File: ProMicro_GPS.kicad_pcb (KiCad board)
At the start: 2 copper layers, 17.8 x 30.5 mm, 30 parts, among them J1 uFL, J2 Coax, U1 MAX-8C, U2 MPU-9250

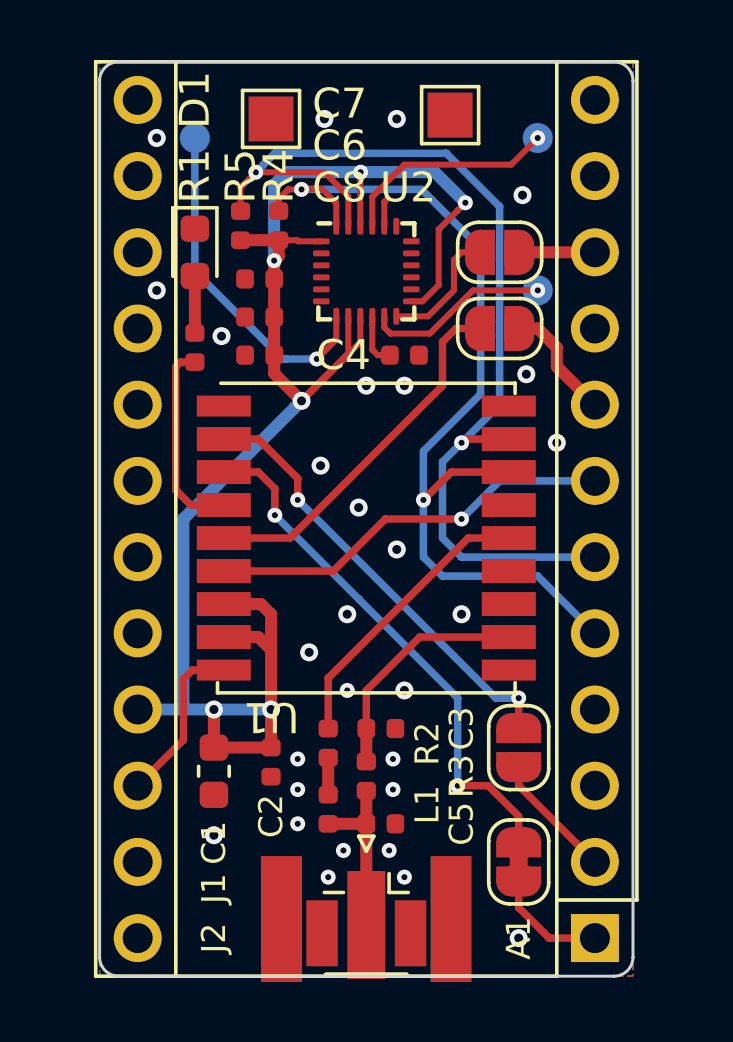
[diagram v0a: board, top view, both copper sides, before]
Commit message: docu in layout
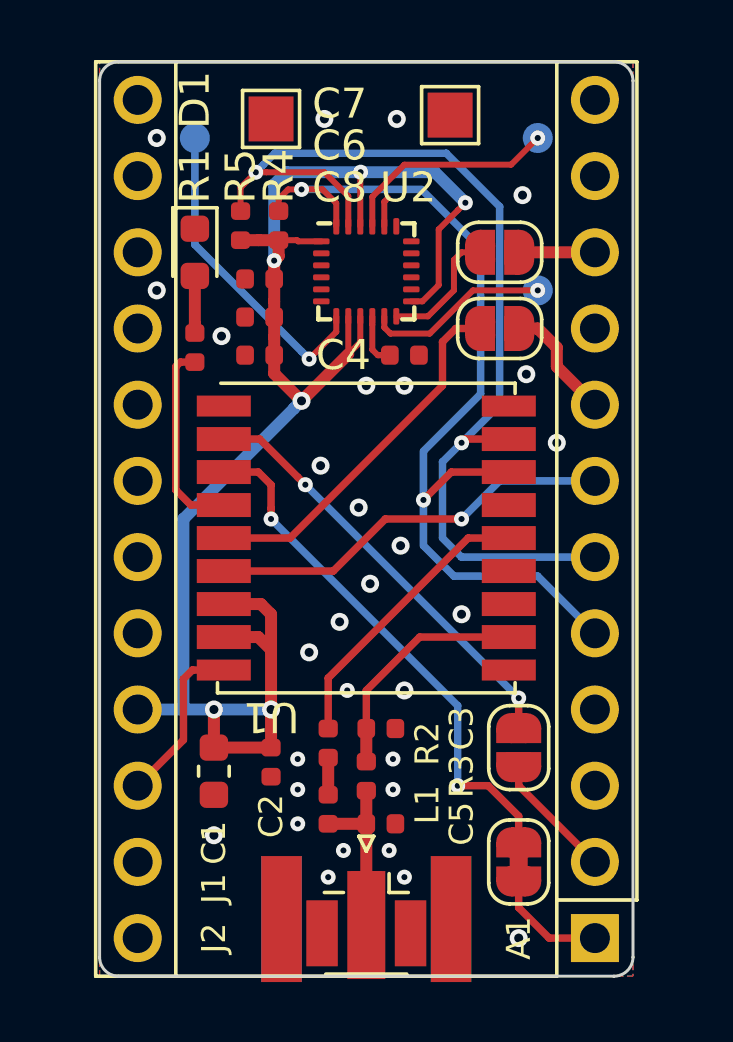
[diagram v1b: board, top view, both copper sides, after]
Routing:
- net Net-(TP3-Pad1): track 11.4 -> 10.7 mm
- net GND: vias 29 -> 30
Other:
- board text added: "3V3"
- board text added: "GND"
- board text added: "GPS_EXTINT"
- board text added: "MPU_INT"
- board text added: "RXD"
- board text added: "SCL"
- board text added: "SDA"
- board text added: "TXD"
- board text added: "VBAT"
- board text added: "v2.3"
- board text added: "~RESET"
- board text removed: "v2.1"

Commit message: variant management
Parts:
- C2: value 100nF -> 100n
- JP1: value SolderJumper_2_Open -> Jumper_NC_Small; footprint Jumper:SolderJumper-2_P1.3mm_Open_RoundedPad1.0x1.5mm -> Jumper:SolderJumper-2_P1.3mm_Bridged_RoundedPad1.0x1.5mm
- JP2: value SolderJumper_2_Open -> Jumper_NO_Small
- JP3: value Jumper_NO_Small -> SolderJumper_2_Open
- JP4: value Jumper_NC_Small -> SolderJumper_2_Open; footprint Jumper:SolderJumper-2_P1.3mm_Bridged_RoundedPad1.0x1.5mm -> Jumper:SolderJumper-2_P1.3mm_Open_RoundedPad1.0x1.5mm
- moved JP4 20.3 mm to (135.3, 88.9), turned to 0 degrees
- moved JP1 17.8 mm to (135.9, 109.2), turned to 90 degrees
- moved JP2 16.5 mm to (135.9, 105.4), turned to 90 degrees
- moved JP3 14.0 mm to (135.3, 91.4), turned to 180 degrees
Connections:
- A1 pad 11: (no net) -> D8
- A1 pad 12: (no net) -> D9
- A1 pad 13: (no net) -> D10
- A1 pad 14: (no net) -> D16
- A1 pad 15: (no net) -> D14
- A1 pad 16: (no net) -> D15
- A1 pad 17: (no net) -> A0
- A1 pad 18: (no net) -> A1
- A1 pad 19: (no net) -> A2
- A1 pad 20: (no net) -> A3
- A1 pad 24: (no net) -> Net-(A1-Pad24)
- A1 pad 3: (no net) -> Net-(A1-Pad3)
- A1 pad 9: (no net) -> D6
- JP1 pad 1: D5 -> D1
- JP2 pad 1: Net-(JP2-Pad1) -> D0
- JP2 pad 2: D7 -> Net-(JP2-Pad2)
- JP3 pad 1: D0 -> D5
- JP4 pad 1: D1 -> Net-(JP4-Pad1)
- JP4 pad 2: Net-(JP4-Pad2) -> D7
- U1 pad 13: (no net) -> Net-(U1-Pad13)
- U1 pad 15: (no net) -> Net-(U1-Pad15)
- U1 pad 18: (no net) -> Net-(U1-Pad18)
- U1 pad 2: Net-(JP3-Pad2) -> Net-(JP2-Pad2)
- U1 pad 3: Net-(JP4-Pad2) -> Net-(JP1-Pad2)
- U1 pad 5: Net-(JP1-Pad2) -> Net-(JP3-Pad2)
- U2 pad 12: Net-(JP2-Pad1) -> Net-(JP4-Pad1)
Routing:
- net Net-(JP4-Pad2): track 17.7 -> 0.00 mm, vias 2 -> 0
- net Net-(JP2-Pad2): track 0.00 -> 14.4 mm, vias 0 -> 2
- net Net-(JP1-Pad2): track 12.3 -> 17.7 mm, vias 0 -> 2
- net Net-(JP4-Pad1): track 0.00 -> 4.27 mm
- net Net-(JP2-Pad1): track 4.27 -> 0.00 mm
- net Net-(JP3-Pad2): track 14.4 -> 12.3 mm, vias 2 -> 0
- net GND: vias 30 -> 32

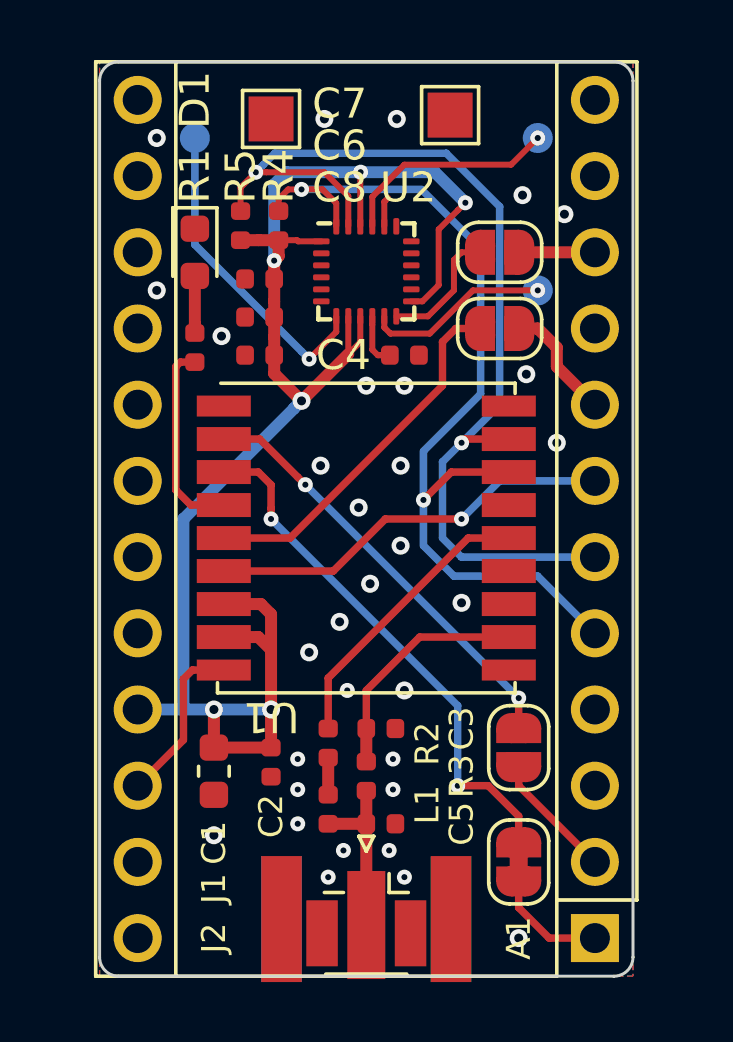
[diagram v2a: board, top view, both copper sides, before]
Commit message: add mouting brackets
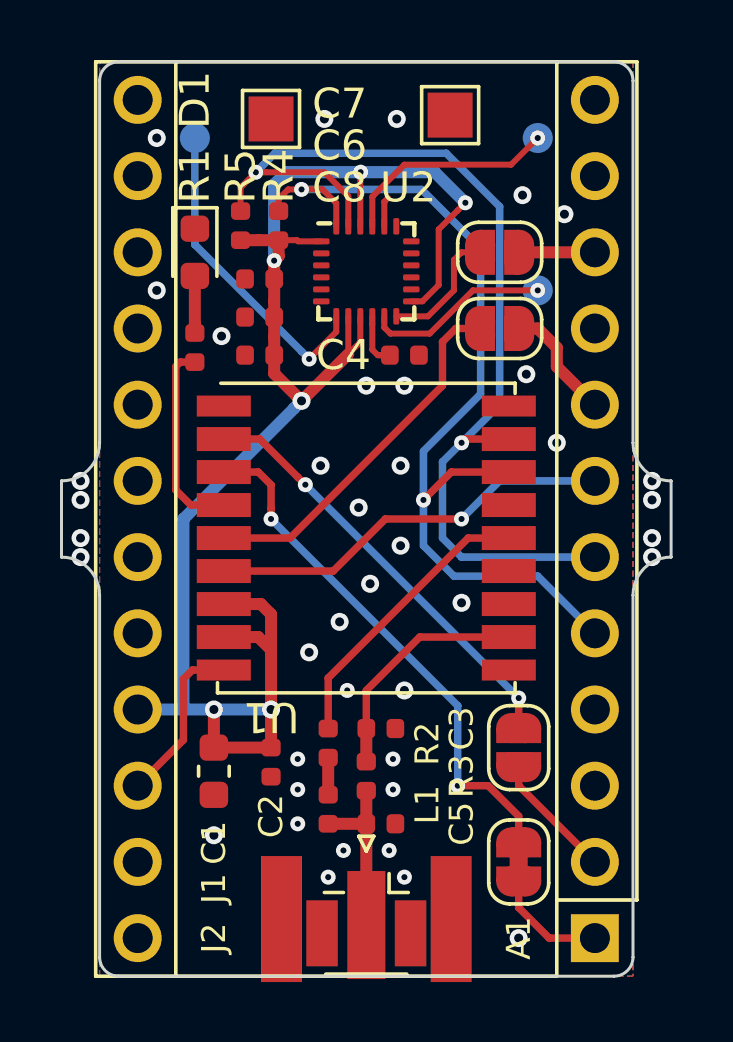
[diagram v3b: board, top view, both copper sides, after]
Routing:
- net (no net): vias 0 -> 8
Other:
- board size 17.8 x 30.5 mm -> 20.3 x 30.5 mm
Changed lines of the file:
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@@
   (general
     (thickness 0.8)
-    (drawings 23)
-    (tracks 214)
+    (drawings 31)
+    (tracks 222)
     (zones 0)
     (modules 30)
@@
     )
   )
+  (gr_line (start 140.97 96.52) (end 140.97 99.06) (layer Edge.Cuts) (width 0.1))
+  (gr_arc (start 140.97 100.33) (end 140.97 99.06) (angle -90) (layer Edge.Cuts) (width 0.1))
+  (gr_line (start 139.7 100.33) (end 139.7 112.395) (layer Edge.Cuts) (width 0.1))
+  (gr_arc (start 140.97 95.25) (end 139.7 95.25) (angle -90) (layer Edge.Cuts) (width 0.1))
+  (gr_line (start 139.7 83.185) (end 139.7 95.25) (layer Edge.Cuts) (width 0.1))
+  (gr_line (start 120.65 99.06) (end 120.65 96.52) (layer Edge.Cuts) (width 0.1))
+  (gr_arc (start 120.65 100.33) (end 121.92 100.33) (angle -90) (layer Edge.Cuts) (width 0.1))
+  (gr_line (start 121.92 112.395) (end 121.92 100.33) (layer Edge.Cuts) (width 0.1))
+  (gr_arc (start 120.65 95.25) (end 120.65 96.52) (angle -90) (layer Edge.Cuts) (width 0.1))
   (gr_text MPU_INT (at 148.59 88.9) (layer Cmts.User)
     (effects (font (size 1 1) (thickness 0.15)))
@@
   (gr_arc (start 139.065 83.185) (end 139.7 83.185) (angle -90) (layer Edge.Cuts) (width 0.1))
   (gr_arc (start 139.065 112.395) (end 139.065 113.03) (angle -90) (layer Edge.Cuts) (width 0.1))
-  (gr_line (start 139.7 83.185) (end 139.7 112.395) (layer Edge.Cuts) (width 0.1))
   (gr_line (start 122.555 82.55) (end 139.065 82.55) (layer Edge.Cuts) (width 0.1))
-  (gr_line (start 121.92 112.395) (end 121.92 83.185) (layer Edge.Cuts) (width 0.1))
+  (gr_line (start 121.92 95.25) (end 121.92 83.185) (layer Edge.Cuts) (width 0.1))
   (gr_line (start 139.065 113.03) (end 122.555 113.03) (layer Edge.Cuts) (width 0.1))
+  (via (at 121.285 98.425) (size 0.6) (drill 0.3) (layers F.Cu B.Cu) (net 0))
+  (via (at 121.285 97.155) (size 0.6) (drill 0.3) (layers F.Cu B.Cu) (net 0))
+  (via (at 121.285 96.52) (size 0.6) (drill 0.3) (layers F.Cu B.Cu) (net 0))
+  (via (at 121.285 99.06) (size 0.6) (drill 0.3) (layers F.Cu B.Cu) (net 0))
+  (via (at 140.335 99.06) (size 0.6) (drill 0.3) (layers F.Cu B.Cu) (net 0))
+  (via (at 140.335 98.425) (size 0.6) (drill 0.3) (layers F.Cu B.Cu) (net 0))
+  (via (at 140.335 96.52) (size 0.6) (drill 0.3) (layers F.Cu B.Cu) (net 0))
+  (via (at 140.335 97.155) (size 0.6) (drill 0.3) (layers F.Cu B.Cu) (net 0))
   (via (at 135.89 111.76) (size 0.6) (drill 0.3) (layers F.Cu B.Cu) (net 1))
   (via (at 130.048 108.839) (size 0.5) (drill 0.2) (layers F.Cu B.Cu) (net 1))
@@
   (segment (start 125.095 91.59) (end 125.095 91.295) (width 0.4) (layer F.Cu) (net 8))
   (segment (start 125.095 89.6875) (end 125.095 91.295) (width 0.4) (layer F.Cu) (net 8))
-  (segment (start 133.7945 91.44) (end 133.35 91.8845) (width 0.25) (layer F.Cu) (net 22))
-  (segment (start 134.605 91.44) (end 133.7945 91.44) (width 0.25) (layer F.Cu) (net 22))
-  (segment (start 133.35 93.345) (end 128.27 98.425) (width 0.25) (layer F.Cu) (net 22))
-  (segment (start 133.35 91.8845) (end 133.35 93.345) (width 0.25) (layer F.Cu) (net 22))
-  (segment (start 128.27 98.425) (end 126.06 98.425) (width 0.25) (layer F.Cu) (net 22))
+  (via (at 133.858 106.68) (size 0.5) (drill 0.2) (layers F.Cu B.Cu) (net 9))
+  (segment (start 133.858 106.68) (end 134.874 106.68) (width 0.25) (layer F.Cu) (net 9))
+  (segment (start 134.874 106.68) (end 135.89 107.696) (width 0.25) (layer F.Cu) (net 9))
+  (segment (start 135.89 107.696) (end 135.89 108.585) (width 0.25) (layer F.Cu) (net 9))
+  (via (at 127.635 97.79) (size 0.5) (drill 0.2) (layers F.Cu B.Cu) (net 9))
+  (segment (start 126.06 96.225) (end 127.21 96.225) (width 0.25) (layer F.Cu) (net 9))
+  (segment (start 127.635 97.436447) (end 127.635 97.79) (width 0.25) (layer F.Cu) (net 9))
+  (segment (start 127.635 96.65) (end 127.635 97.436447) (width 0.25) (layer F.Cu) (net 9))
+  (segment (start 127.21 96.225) (end 127.635 96.65) (width 0.25) (layer F.Cu) (net 9))
+  (segment (start 133.858 104.013) (end 127.635 97.79) (width 0.25) (layer B.Cu) (net 9))
+  (segment (start 133.858 106.68) (end 133.858 104.013) (width 0.25) (layer B.Cu) (net 9))
   (segment (start 135.905 88.9) (end 138.43 88.9) (width 0.4) (layer F.Cu) (net 10))
   (segment (start 135.905 91.44) (end 136.525 91.44) (width 0.4) (layer F.Cu) (net 11))
@@
   (segment (start 130.81 106.8475) (end 130.81 107.95) (width 0.4) (layer F.Cu) (net 17))
   (segment (start 129.54 107.95) (end 130.81 107.95) (width 0.4) (layer F.Cu) (net 17))
-  (segment (start 133.985 88.9) (end 134.605 88.9) (width 0.2) (layer F.Cu) (net 37))
-  (segment (start 131.81 91.035) (end 132.866 91.035) (width 0.2) (layer F.Cu) (net 37))
-  (segment (start 133.731 89.154) (end 133.985 88.9) (width 0.2) (layer F.Cu) (net 37))
-  (segment (start 133.731 90.17) (end 133.731 89.154) (width 0.2) (layer F.Cu) (net 37))
-  (segment (start 132.866 91.035) (end 133.731 90.17) (width 0.2) (layer F.Cu) (net 37))
   (segment (start 124.96 97.325) (end 126.06 97.325) (width 0.25) (layer F.Cu) (net 18))
   (segment (start 124.61 92.56) (end 124.46 92.71) (width 0.25) (layer F.Cu) (net 18))
@@
   (segment (start 129.81 91.035) (end 129.81 91.551) (width 0.2) (layer F.Cu) (net 21))
   (segment (start 125.095 85.09) (end 125.095 88.646) (width 0.25) (layer B.Cu) (net 21))
+  (segment (start 133.7945 91.44) (end 133.35 91.8845) (width 0.25) (layer F.Cu) (net 22))
+  (segment (start 134.605 91.44) (end 133.7945 91.44) (width 0.25) (layer F.Cu) (net 22))
+  (segment (start 133.35 93.345) (end 128.27 98.425) (width 0.25) (layer F.Cu) (net 22))
+  (segment (start 133.35 91.8845) (end 133.35 93.345) (width 0.25) (layer F.Cu) (net 22))
+  (segment (start 128.27 98.425) (end 126.06 98.425) (width 0.25) (layer F.Cu) (net 22))
   (via (at 135.89 103.759) (size 0.5) (drill 0.2) (layers F.Cu B.Cu) (net 36))
   (segment (start 135.89 103.759) (end 135.89 104.775) (width 0.25) (layer F.Cu) (net 36))
@@
   (segment (start 128.528001 96.397001) (end 128.778 96.647) (width 0.25) (layer F.Cu) (net 36))
   (segment (start 127.256 95.125) (end 128.528001 96.397001) (width 0.25) (layer F.Cu) (net 36))
-  (via (at 133.858 106.68) (size 0.5) (drill 0.2) (layers F.Cu B.Cu) (net 9))
-  (segment (start 133.858 106.68) (end 134.874 106.68) (width 0.25) (layer F.Cu) (net 9))
-  (segment (start 134.874 106.68) (end 135.89 107.696) (width 0.25) (layer F.Cu) (net 9))
-  (segment (start 135.89 107.696) (end 135.89 108.585) (width 0.25) (layer F.Cu) (net 9))
-  (via (at 127.635 97.79) (size 0.5) (drill 0.2) (layers F.Cu B.Cu) (net 9))
-  (segment (start 126.06 96.225) (end 127.21 96.225) (width 0.25) (layer F.Cu) (net 9))
-  (segment (start 127.635 97.436447) (end 127.635 97.79) (width 0.25) (layer F.Cu) (net 9))
-  (segment (start 127.635 96.65) (end 127.635 97.436447) (width 0.25) (layer F.Cu) (net 9))
-  (segment (start 127.21 96.225) (end 127.635 96.65) (width 0.25) (layer F.Cu) (net 9))
-  (segment (start 133.858 104.013) (end 127.635 97.79) (width 0.25) (layer B.Cu) (net 9))
-  (segment (start 133.858 106.68) (end 133.858 104.013) (width 0.25) (layer B.Cu) (net 9))
+  (segment (start 133.985 88.9) (end 134.605 88.9) (width 0.2) (layer F.Cu) (net 37))
+  (segment (start 131.81 91.035) (end 132.866 91.035) (width 0.2) (layer F.Cu) (net 37))
+  (segment (start 133.731 89.154) (end 133.985 88.9) (width 0.2) (layer F.Cu) (net 37))
+  (segment (start 133.731 90.17) (end 133.731 89.154) (width 0.2) (layer F.Cu) (net 37))
+  (segment (start 132.866 91.035) (end 133.731 90.17) (width 0.2) (layer F.Cu) (net 37))
   (zone (net 1) (net_name GND) (layer F.Cu) (hatch edge 0.508)
     (connect_pads (clearance 0.2))
